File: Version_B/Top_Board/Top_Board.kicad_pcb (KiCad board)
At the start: 2 copper layers, 78.7 x 31 mm, 13 parts, among them J1 90_Deg_Conn, J2 ADS1015, J4 90_Deg_Conn, U1 T-Display-S3

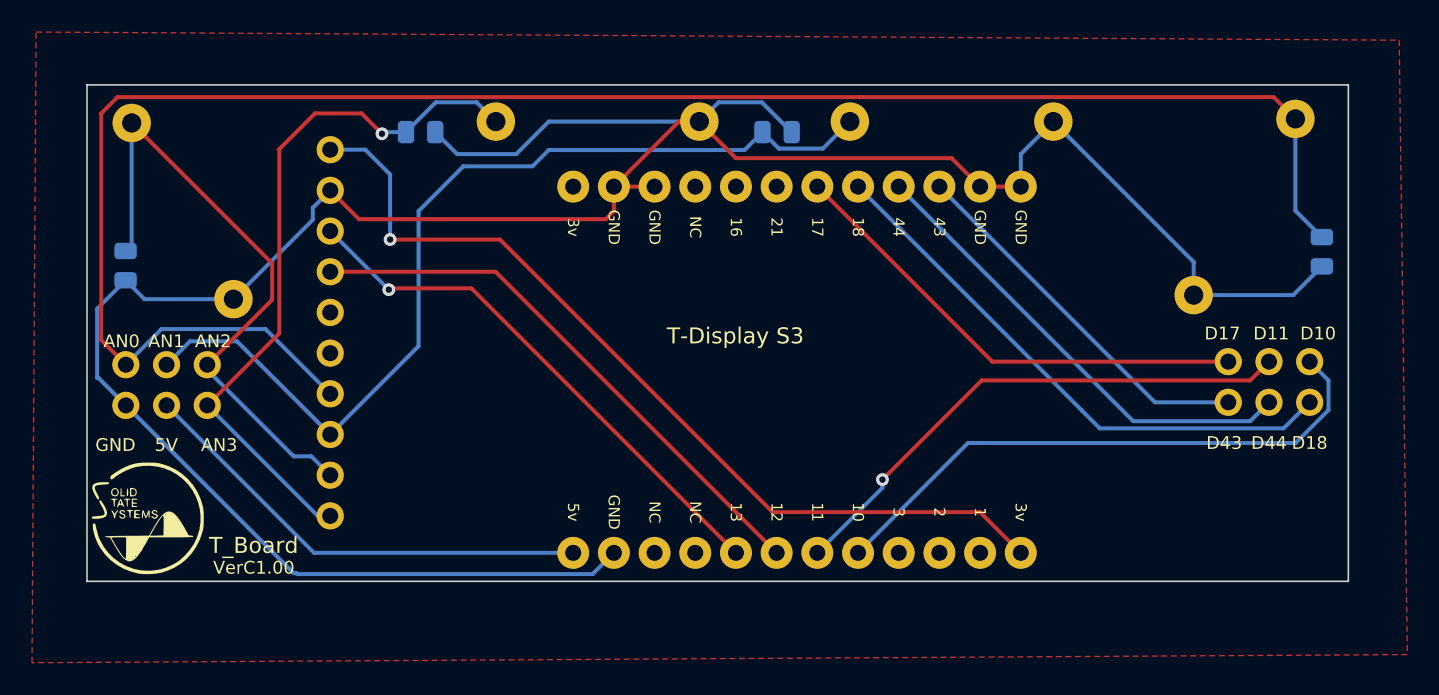
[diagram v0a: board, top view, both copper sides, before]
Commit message: ads1015 on bottom board and aesthetic changes
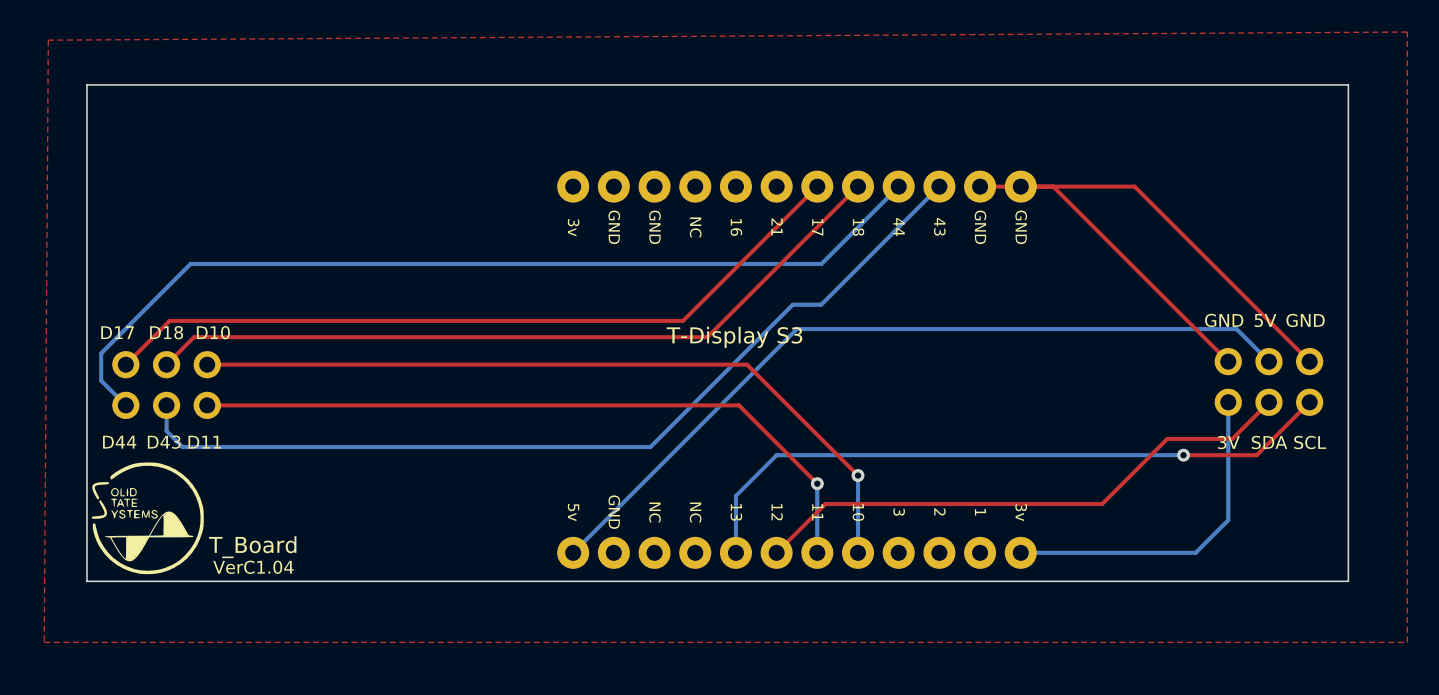
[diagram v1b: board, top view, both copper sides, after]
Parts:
- removed the J2 at (128.3, 105.6)
- removed R1, R4, R5, R7: R, Resistor_SMD:R_0805_2012Metric
- removed R2, R3, R6, R8: R, Resistor_THT:R_Axial_DIN0411_L9.9mm_D3.6mm_P12.70mm_Horizontal
- added G***: LOGO, top_lib:my_logo, B.Cu at (115.6, 80.5)
- renumbered J4 to J2
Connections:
- J1 pad 1: AN0 -> D17
- J1 pad 2: GND -> D44
- J1 pad 3: AN1 -> D18
- J1 pad 4: 5V -> D43
- J1 pad 5: AN2 -> D10
- J1 pad 6: AN3 -> D11
- J2 pad 1: D17 -> GND
- J2 pad 2: D43 -> 3V
- J2 pad 3: D11 -> 5V
- J2 pad 4: D44 -> SDA
- J2 pad 5: D10 -> GND
- J2 pad 6: D18 -> SCL
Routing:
- net GND: track 165.8 -> 42.6 mm
- net AN0: track 115.3 -> 0.00 mm
- net AN1: track 59.6 -> 0.00 mm
- net AN3: track 44.7 -> 0.00 mm, vias 1 -> 0
- net AN2: track 39.3 -> 0.00 mm
- net 3V: track 55.9 -> 21.2 mm, vias 1 -> 0
- net D43: track 23.6 -> 57.0 mm
- net D44: track 29.7 -> 58.0 mm
- net 5V: track 29.2 -> 50.1 mm
- net D17: track 30.2 -> 47.8 mm
- net D18: track 35.1 -> 47.8 mm
- net D10: track 36.6 -> 48.3 mm, vias 0 -> 1
- net D11: track 33.4 -> 44.4 mm
- net SCL: track 33.7 -> 41.8 mm
- net SDA: track 35.1 -> 34.6 mm
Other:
- board text added: "3V"
- board text added: "SCL"
- board text added: "SDA"
- board text added: "VerC1.04"
- board text removed: "3.9 Mohm"
- board text removed: "3.9 Mohms"
- board text removed: "ADS1015"
- board text removed: "AN0"
- board text removed: "AN1"
- board text removed: "AN2"
- board text removed: "AN3"
- board text removed: "D5"
- board text removed: "VerC1.00"
